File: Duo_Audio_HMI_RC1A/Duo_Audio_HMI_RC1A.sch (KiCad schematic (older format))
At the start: 0 parts

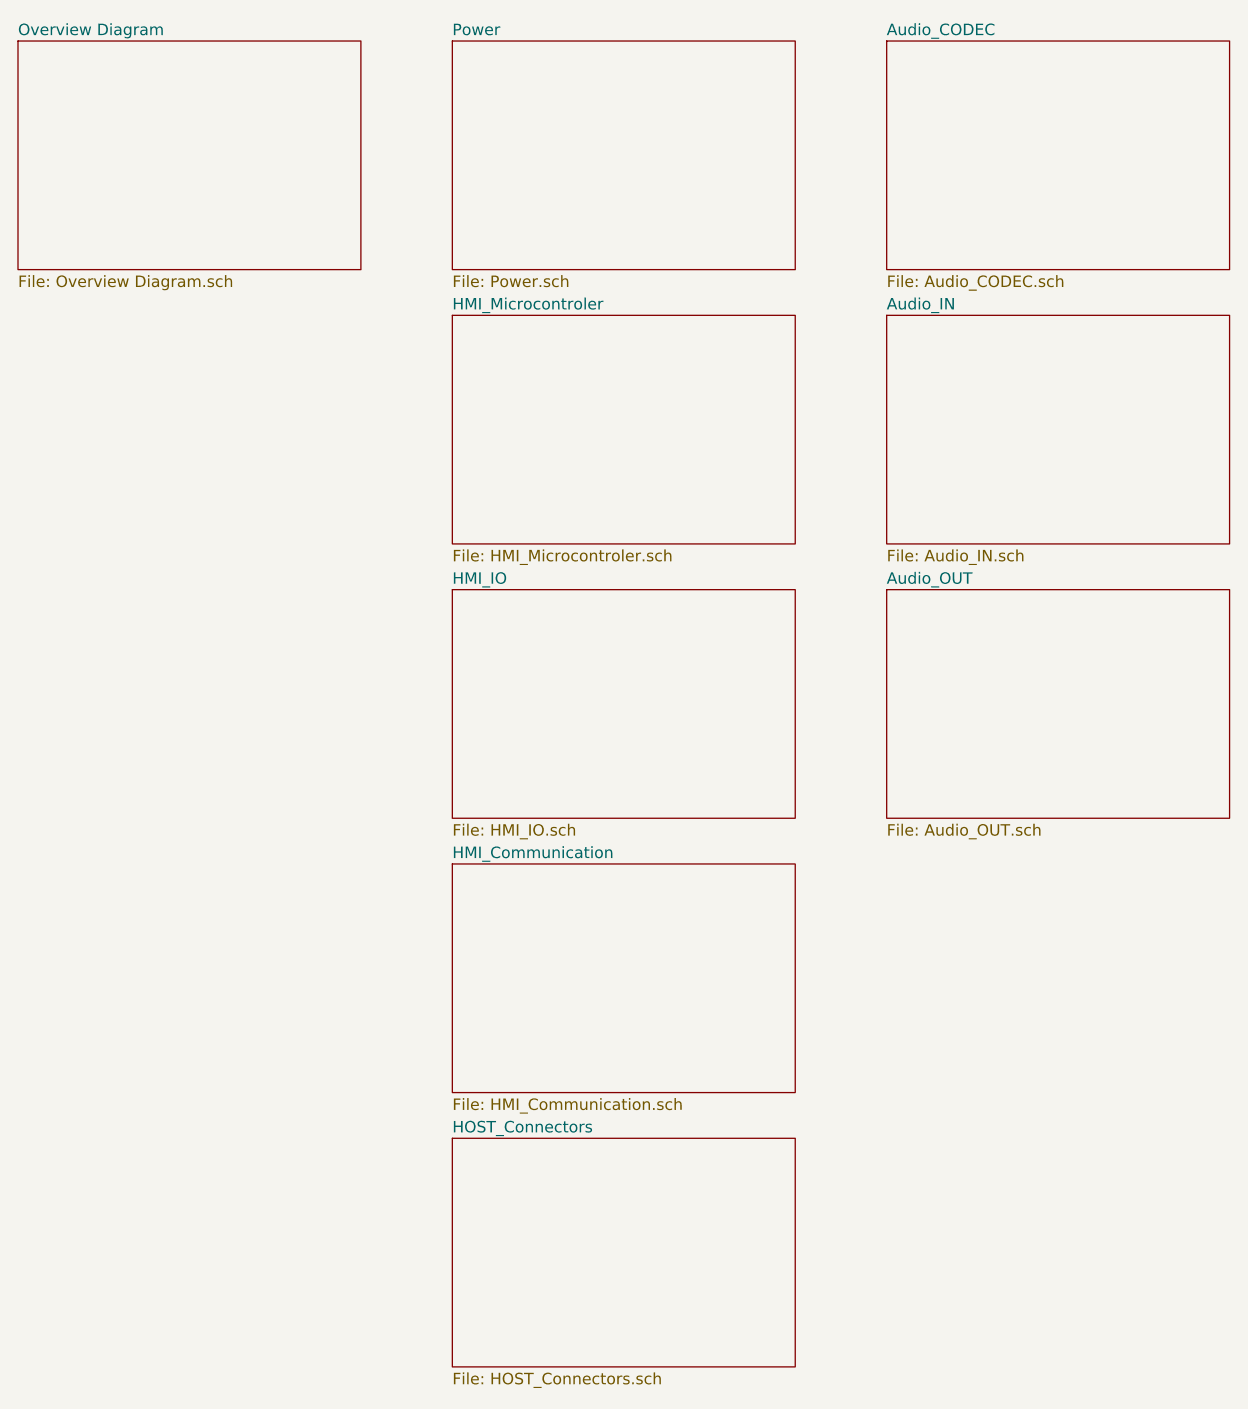
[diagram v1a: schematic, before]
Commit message: Major changes on hardware architecture. Migrating to a HMI separated board. HMI schematic finalized.
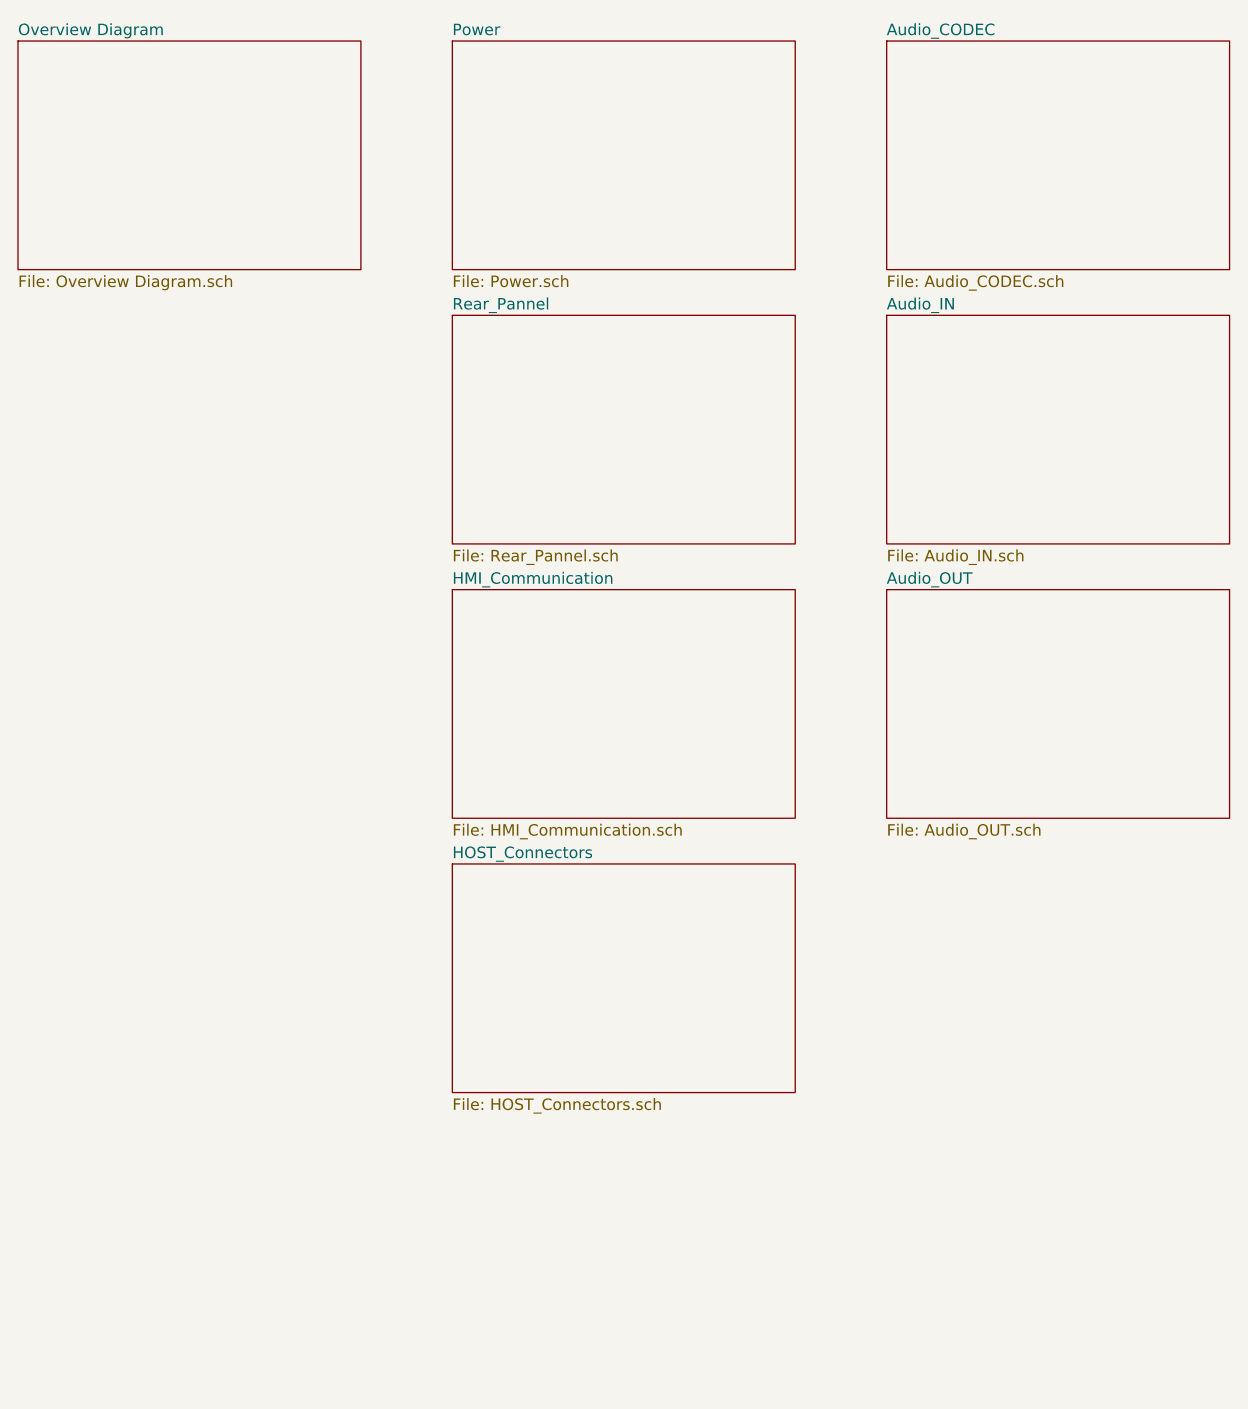
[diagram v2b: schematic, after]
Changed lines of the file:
@@
 LIBS:Duo_Audio_HMI_RC1A
 LIBS:Duo_Audio_HMI_RC1A-cache
-EELAYER 27 0
+EELAYER 24 0
 EELAYER END
 $Descr A4 11693 8268
 encoding utf-8
-Sheet 1 10
+Sheet 1 9
 Title "MOD Duo Baseboard RC1A"
 Date "20 may 2014"
@@
 $Sheet
 S 3450 3650 1500 1000
-U 531F6D38
-F0 "HMI_IO" 50
-F1 "HMI_IO.sch" 50
-$EndSheet
-$Sheet
-S 3450 2450 1500 1000
-U 531FDB5F
-F0 "HMI_Microcontroler" 50
-F1 "HMI_Microcontroler.sch" 50
-$EndSheet
-$Sheet
-S 3450 4850 1500 1000
 U 53216662
 F0 "HMI_Communication" 50
@@
 $EndSheet
 $Sheet
-S 3450 6050 1500 1000
+S 3450 4850 1500 1000
 U 5321AB9D
 F0 "HOST_Connectors" 50
@@
 F1 "Audio_CODEC.sch" 50
 $EndSheet
+$Sheet
+S 3450 2450 1500 1000
+U 537BCE69
+F0 "Rear_Pannel" 50
+F1 "Rear_Pannel.sch" 50
+$EndSheet
 $EndSCHEMATC
